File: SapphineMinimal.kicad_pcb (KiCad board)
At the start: 4 copper layers, 54.6 x 61 mm, 149 parts, among them IC301 DLHR-F50D-E1BD-C-NAV8, J201 JST, J401 503182-1852, J501 Conn_02x05_Odd_Even, J502 Conn_01x03_Male, J503 USB_B_Micro, J504 Conn_01x05_Male, J505 Conn_01x08_Female, J506 Conn_01x08_Female, J507 Conn_01x04_Male, J701 Conn_01x04_Male, J702 Conn_01x01_Male, J703 Conn_01x06_Male, Q201 BC857BS, Q202 IRLML6402TRPBF, SW501 EVQP7C01P, SW601 EVQP7C01P, U201 TPS62150, U202 INA219BIDR, U301 LIS331DLHTR, U401 TPS22860DBVR, U501 ATSAMD21E18A-AUT, U502 BMP388, U503 MB85RS1MT, U601 DS3231SN, U701 TPS22860DBVR

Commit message: 3d references'
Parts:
- SW501, SW601: value EVQP7C01P -> EVQP7C/L_PAN
- U301: value LIS331DLHTR -> LGA-16_3x3x1mm_STM
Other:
- net class Default removed
- net class Ground removed
- net class Power removed

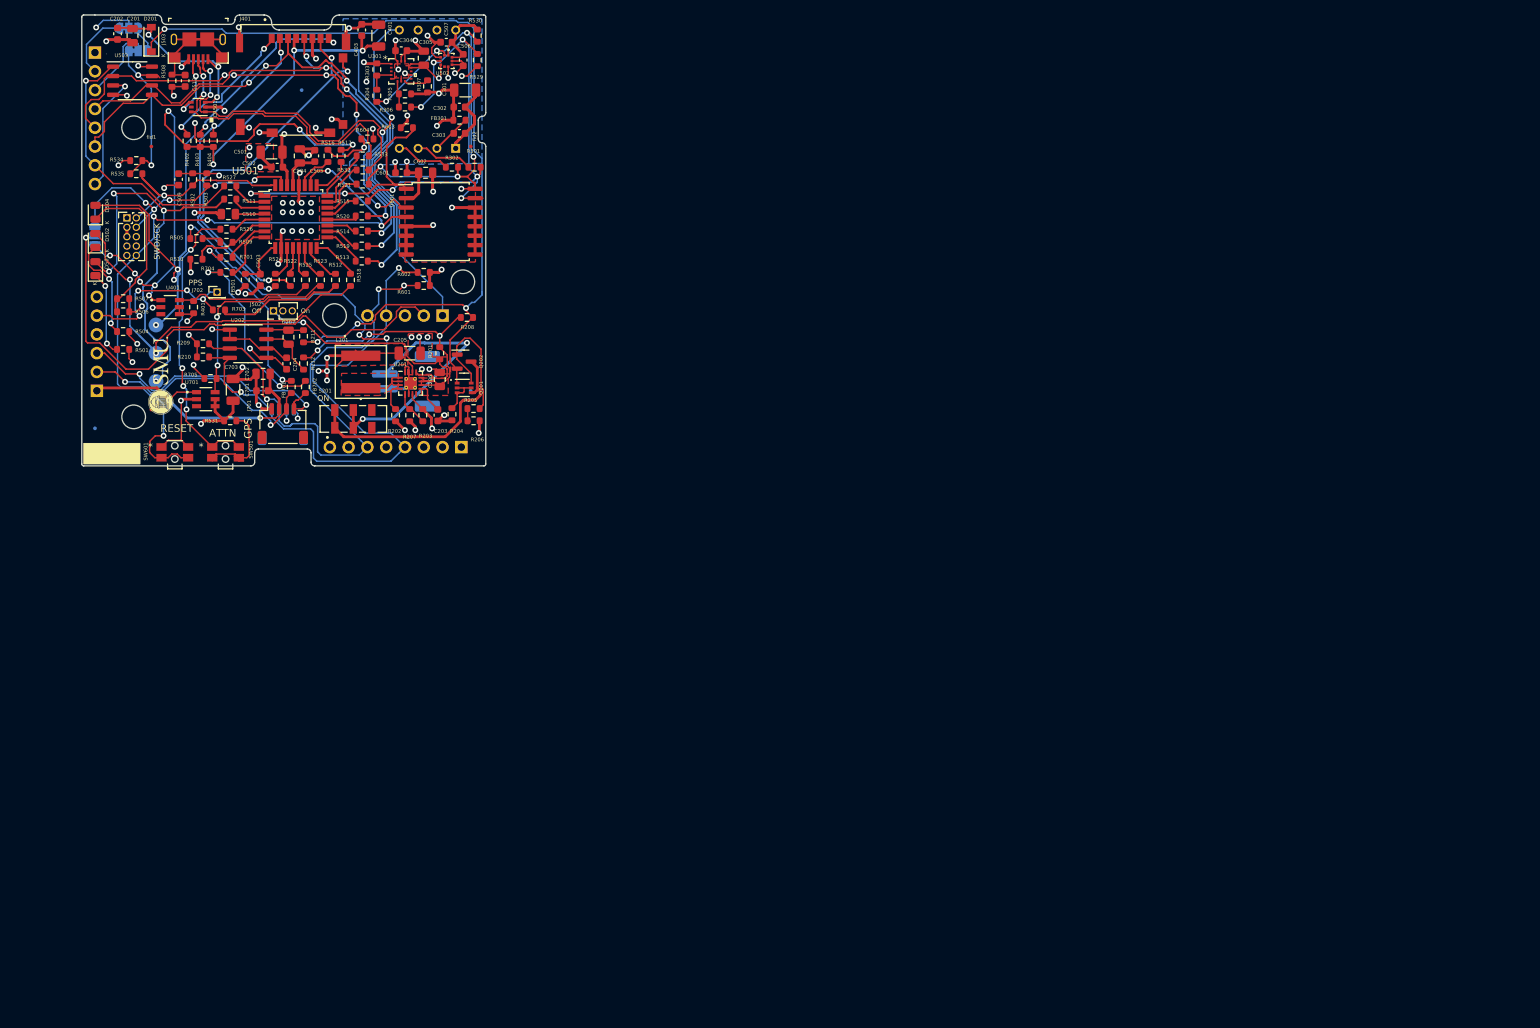
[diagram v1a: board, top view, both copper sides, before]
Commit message: Footprints complete. Starting layout
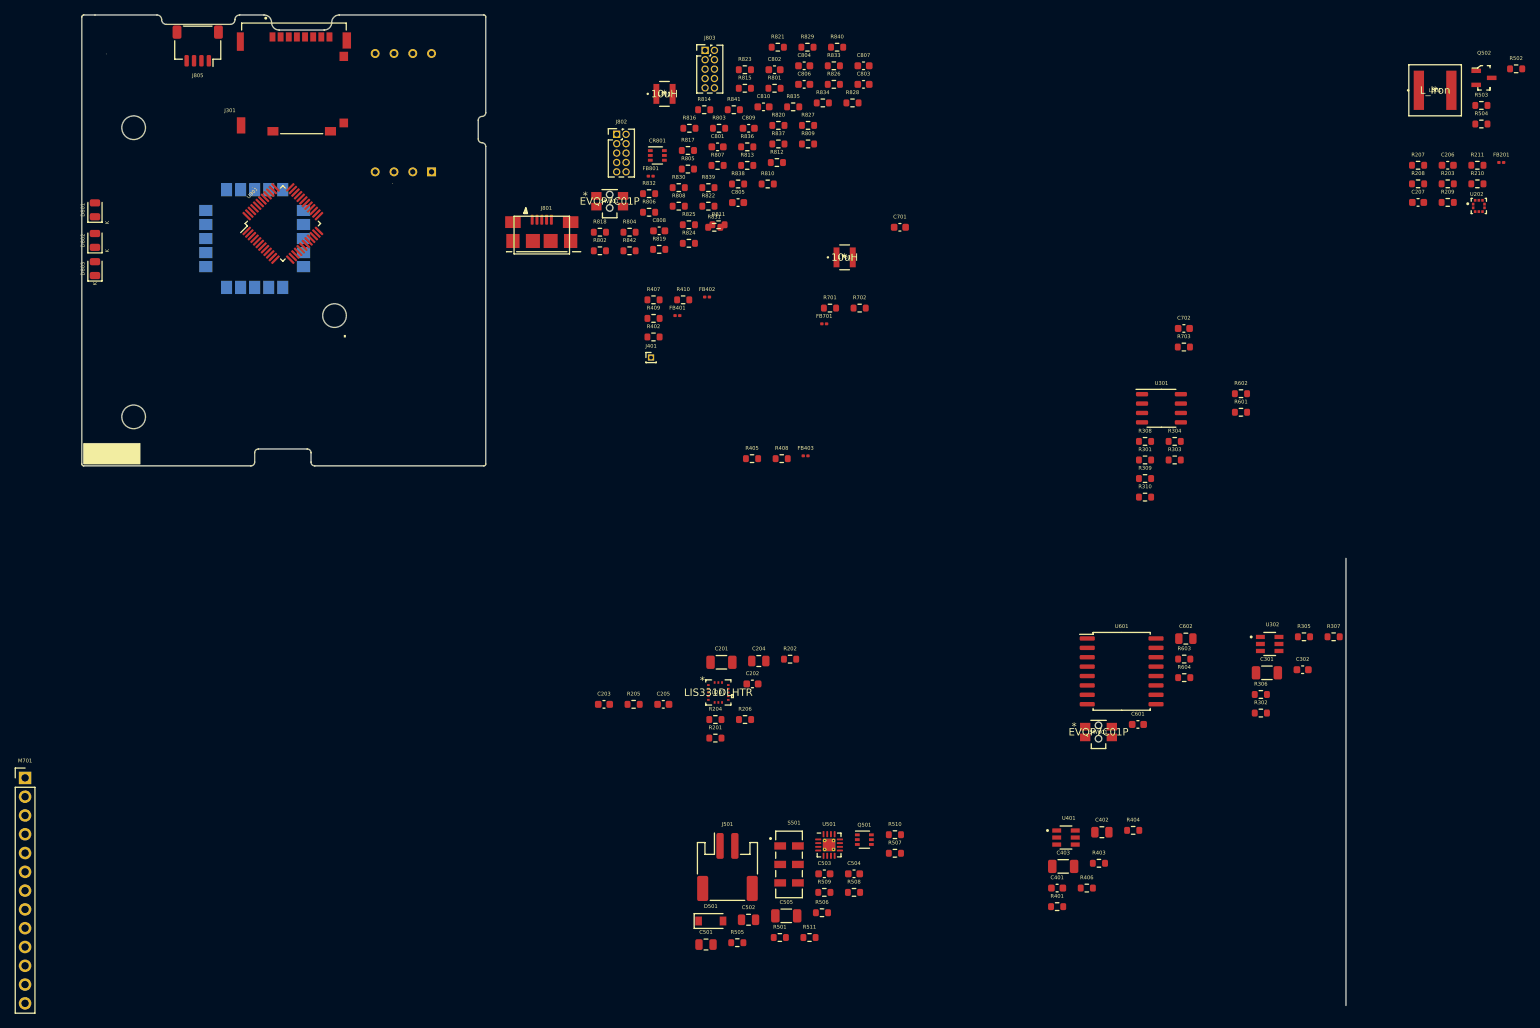
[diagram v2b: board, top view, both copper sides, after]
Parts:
- removed C303, C304, C506, C507, C509, C512: 100nF, Capacitor_SMD:C_0603_1608Metric
- removed C305: 10uF, Capacitor_SMD:C_0805_2012Metric
- removed C510: 1uF, Capacitor_SMD:C_0805_2012Metric
- removed C703: 22uF, Capacitor_SMD:C_1206_3216Metric
- removed CR501: TPD4E1U06DCKR, Package_TO_SOT_SMD:SOT-363_SC-70-6
- removed D201: MBR180, Diode_SMD:D_SOD-123
- removed D502: RED LED, LED_SMD:LED_0805_2012Metric
- removed D504: GREEN LED, LED_SMD:LED_0805_2012Metric
- removed FB301, FB501, FB702: 600, Resistor_SMD:R_0603_1608Metric
- removed G***: LOGO, LOGOS:SMU_Logo
- removed G***: LOGO, SapphineMinimal:SMU_Logo_Big2
- removed IC301: DLHR-F50D-E1BD-C-NAV8, SapphineMinimal:DLHRF50DE1BDCNAV8
- removed J201: JST, Connector_JST:JST_PH_S2B-PH-SM4-TB_1x02-1MP_P2.00mm_Horizontal
- removed J502: Conn_01x03_Male, Connector_PinHeader_1.27mm:PinHeader_1x03_P1.27mm_Vertical
- removed J503: USB_B_Micro, digikey-footprints:USB_Micro_B_Female_10118193-0001LF
- removed J504: Conn_01x05_Male, Connector_PinSocket_2.54mm:PinSocket_1x05_P2.54mm_Vertical
- removed J505, J506: Conn_01x08_Female, Connector_PinSocket_2.54mm:PinSocket_1x08_P2.54mm_Vertical
- removed J507, J701: Conn_01x04_Male, Connector_JST:JST_SH_SM04B-SRSS-TB_1x04-1MP_P1.00mm_Horizontal
- removed J702: Conn_01x01_Male, Connector_PinHeader_1.27mm:PinHeader_1x01_P1.27mm_Vertical
- removed J703: Conn_01x06_Male, Connector_PinHeader_2.54mm:PinHeader_1x06_P2.54mm_Horizontal
- removed JP501, JP502: Jumper_3_Bridged12, Jumper:SolderJumper-3_P1.3mm_Bridged12_RoundedPad1.0x1.5mm_NumberLabels
- removed JP503: SolderJumper_3_Open, Jumper:SolderJumper-3_P1.3mm_Open_RoundedPad1.0x1.5mm_NumberLabels
- removed L201: 2.2uH, SapphineMinimal:74439344022
- removed Q201: BC857BS, Package_TO_SOT_SMD:SOT-363_SC-70-6
- removed Q202: IRLML6402TRPBF, Package_TO_SOT_SMD:SOT-23
- removed R212: 10, Resistor_SMD:R_0603_1608Metric
- removed R512, R513, R515, R516, R517, R518, R519, R520, R521, R523, R524, R525, R526, R527, R532, R533, R535, R704: 47, Resistor_SMD:R_0603_1608Metric
- removed R514, R522, R531: 2K, Resistor_SMD:R_0603_1608Metric
- removed R529, R530: 4K75, Resistor_SMD:R_0603_1608Metric
- removed R534: 10K, Resistor_SMD:R_0603_1608Metric
- removed R705: 100K, Resistor_SMD:R_0603_1608Metric
- removed the REF** at (128.5, 102.1)
- removed S201: JS202011JCQN, SapphineMinimal:SW_JS202011JCQN
- removed SW501: EVQP7C/L_PAN, SapphineMinimal:EVQP7C01P
- removed TP501, TP502, TP503: TestPoint, TestPoint:TestPoint_Pad_D2.0mm
- removed U502: BMP388, SapphineMinimal:PQFN50P200X200X80-10N
- removed U503: MB85RS1MT, Package_SO:SOP-8_3.9x4.9mm_P1.27mm
- removed U701: TPS22860DBVR, SapphineMinimal:SOT95P280X145-6N
- removed fid1 (x2), fid2, fid4, fid5, fid6: Fiducial_0.5mm_Mask1mm, Fiducial:Fiducial_0.5mm_Mask1mm
- added C402: 10uF, Capacitor_SMD:C_0805_2012Metric, F.Cu at (214.9, 176.5)
- added C801: 100nF, Capacitor_SMD:C_0603_1608Metric, F.Cu at (162.9, 83.9)
- added C802: 1uf, Capacitor_SMD:C_0603_1608Metric, F.Cu at (170.6, 73.4)
- added C803: 100pF, Capacitor_SMD:C_0603_1608Metric, F.Cu at (182.6, 75.4)
- added C804: 1uf, Capacitor_SMD:C_0603_1608Metric, F.Cu at (174.6, 72.9)
- added C805: 22uF, Capacitor_SMD:C_0603_1608Metric, F.Cu at (165.7, 91.4)
- added C806: 100nF, Capacitor_SMD:C_0603_1608Metric, F.Cu at (174.6, 75.4)
- added C807: 100nF, Capacitor_SMD:C_0603_1608Metric, F.Cu at (182.6, 72.9)
- added C808: 22uF, Capacitor_SMD:C_0603_1608Metric, F.Cu at (155.0, 95.2)
- added C809: 100nF, Capacitor_SMD:C_0603_1608Metric, F.Cu at (167.1, 81.4)
- added C810: 100nF, Capacitor_SMD:C_0603_1608Metric, F.Cu at (169.1, 78.5)
- added CR801: TPD4E1U06DCKR, Package_TO_SOT_SMD:SOT-363_SC-70-6, F.Cu at (154.8, 85.0)
- added D801: RED LED, LED_SMD:LED_0805_2012Metric, F.Cu at (78.7, 92.4)
- added D802: RED LED, LED_SMD:LED_0805_2012Metric, F.Cu at (78.7, 96.5)
- added D803: GREEN LED, LED_SMD:LED_0805_2012Metric, F.Cu at (78.7, 100.3)
- added FB201: FerriteBead, Inductor_SMD:L_0201_0603Metric, F.Cu at (268.9, 86.0)
- added FB401: FerriteBead, Inductor_SMD:L_0201_0603Metric, F.Cu at (157.5, 106.7)
- added FB402: FerriteBead, Inductor_SMD:L_0201_0603Metric, F.Cu at (161.5, 104.2)
- added FB403: FerriteBead, Inductor_SMD:L_0201_0603Metric, F.Cu at (174.8, 125.6)
- added FB801: FerriteBead, Inductor_SMD:L_0201_0603Metric, F.Cu at (153.9, 87.8)
- added IC201: DLHR-F50D-E1BD-C-NAV8, SapphineMinimal:DLHRF50DE1BDCNAV8, B.Cu at (124.2, 87.2)
- added J301: 503182-1852, SapphineMinimal:MOLEX_503182-1852, F.Cu at (105.6, 75.4)
- added J801: USB_B_Micro, SapphineMinimal:uUSB_B, F.Cu at (139.1, 96.6)
- added J802: Conn_02x05_Odd_Even, Connector_PinHeader_1.27mm:PinHeader_2x05_P1.27mm_Vertical, F.Cu at (149.3, 82.2)
- added J803: Conn_02x05_Odd_Even, Connector_PinHeader_1.27mm:PinHeader_2x05_P1.27mm_Vertical, F.Cu at (161.2, 70.8)
- added J805: Conn_01x04_Male, Connector_JST:JST_SH_SM04B-SRSS-TB_1x04-1MP_P1.00mm_Horizontal, F.Cu at (92.6, 70.2)
- added L501: L_Iron, SapphineMinimal:74439344022, F.Cu at (259.9, 76.2)
- added L701: 10uH, SapphineMinimal:NR3012T100M, F.Cu at (180.1, 98.8)
- added L801: 10uH, SapphineMinimal:NR3012T100M, F.Cu at (155.7, 76.7)
- added M701: AdafruitWINC1500, Connector_PinHeader_2.54mm:PinHeader_1x13_P2.54mm_Vertical, F.Cu at (69.3, 169.2)
- added Q501: BC857BS, Package_TO_SOT_SMD:SOT-363_SC-70-6, F.Cu at (182.8, 177.5)
- added Q502: IRLML6402TRPBF, digikey-footprints:SOT-23-3, F.Cu at (266.5, 74.5)
- added R308: 47, Resistor_SMD:R_0603_1608Metric, F.Cu at (220.7, 123.7)
- added R309: 47, Resistor_SMD:R_0603_1608Metric, F.Cu at (220.7, 128.7)
- added R310: 0, Resistor_SMD:R_0603_1608Metric, F.Cu at (220.7, 131.2)
- added R405: 47, Resistor_SMD:R_0603_1608Metric, F.Cu at (167.6, 126.0)
- added R406: 100K, Resistor_SMD:R_0603_1608Metric, F.Cu at (212.8, 184.1)
- added R407: 47, Resistor_SMD:R_0603_1608Metric, F.Cu at (154.2, 104.5)
- added R408: 47, Resistor_SMD:R_0603_1608Metric, F.Cu at (171.6, 126.0)
- added R409: open, Resistor_SMD:R_0603_1608Metric, F.Cu at (154.2, 107.1)
- added R410: open, Resistor_SMD:R_0603_1608Metric, F.Cu at (158.3, 104.5)
- added R702: 47, Resistor_SMD:R_0603_1608Metric, F.Cu at (182.1, 105.7)
- added R801: 4K75, Resistor_SMD:R_0603_1608Metric, F.Cu at (170.6, 76.0)
- added R802: 2K, Resistor_SMD:R_0603_1608Metric, F.Cu at (147.0, 97.9)
- added R803: 2K, Resistor_SMD:R_0603_1608Metric, F.Cu at (163.1, 81.4)
- added R804: 2K, Resistor_SMD:R_0603_1608Metric, F.Cu at (151.0, 95.4)
- added R805: 2K, Resistor_SMD:R_0603_1608Metric, F.Cu at (158.9, 86.9)
- added R806: 2K, Resistor_SMD:R_0603_1608Metric, F.Cu at (153.7, 92.7)
- added R807: 4K75, Resistor_SMD:R_0603_1608Metric, F.Cu at (162.9, 86.4)
- added R808: 4K75, Resistor_SMD:R_0603_1608Metric, F.Cu at (157.7, 91.9)
- added R809: 47, Resistor_SMD:R_0603_1608Metric, F.Cu at (175.1, 83.5)
- added R810: 330, Resistor_SMD:R_0603_1608Metric, F.Cu at (169.7, 88.9)
- added R811: 2k2, Resistor_SMD:R_0603_1608Metric, F.Cu at (163.0, 94.4)
- added R812: 47, Resistor_SMD:R_0603_1608Metric, F.Cu at (170.9, 86.0)
- added R813: 47, Resistor_SMD:R_0603_1608Metric, F.Cu at (166.9, 86.4)
- added R814: 47, Resistor_SMD:R_0603_1608Metric, F.Cu at (161.1, 78.8)
- added R815: 47, Resistor_SMD:R_0603_1608Metric, F.Cu at (166.6, 76.0)
- added R816: 47, Resistor_SMD:R_0603_1608Metric, F.Cu at (159.1, 81.4)
- added R817: 47, Resistor_SMD:R_0603_1608Metric, F.Cu at (158.9, 84.4)
- added R818: 47, Resistor_SMD:R_0603_1608Metric, F.Cu at (147.0, 95.4)
- added R819: 47, Resistor_SMD:R_0603_1608Metric, F.Cu at (155.0, 97.7)
- added R820: 47, Resistor_SMD:R_0603_1608Metric, F.Cu at (171.1, 81.0)
- added R821: 47, Resistor_SMD:R_0603_1608Metric, F.Cu at (171.1, 70.4)
- added R822: 47, Resistor_SMD:R_0603_1608Metric, F.Cu at (161.7, 91.9)
- added R823: 47, Resistor_SMD:R_0603_1608Metric, F.Cu at (166.6, 73.4)
- added R824: 47, Resistor_SMD:R_0603_1608Metric, F.Cu at (159.0, 96.9)
- added R825: 47, Resistor_SMD:R_0603_1608Metric, F.Cu at (159.0, 94.4)
- added R826: 47, Resistor_SMD:R_0603_1608Metric, F.Cu at (178.6, 75.4)
- added R827: 47, Resistor_SMD:R_0603_1608Metric, F.Cu at (175.1, 81.0)
- added R828: 47, Resistor_SMD:R_0603_1608Metric, F.Cu at (181.2, 77.9)
- added R829: 47, Resistor_SMD:R_0603_1608Metric, F.Cu at (175.1, 70.4)
- added R830: 47, Resistor_SMD:R_0603_1608Metric, F.Cu at (157.7, 89.4)
- added R831: 47, Resistor_SMD:R_0603_1608Metric, F.Cu at (162.5, 94.7)
- added R832: 47, Resistor_SMD:R_0603_1608Metric, F.Cu at (153.7, 90.2)
- added R833: 47, Resistor_SMD:R_0603_1608Metric, F.Cu at (178.6, 72.9)
- added R834: 47, Resistor_SMD:R_0603_1608Metric, F.Cu at (177.1, 77.9)
- added R835: 47, Resistor_SMD:R_0603_1608Metric, F.Cu at (173.1, 78.5)
- added R836: 47, Resistor_SMD:R_0603_1608Metric, F.Cu at (166.9, 83.9)
- added R837: 47, Resistor_SMD:R_0603_1608Metric, F.Cu at (171.1, 83.5)
- added R838: 47, Resistor_SMD:R_0603_1608Metric, F.Cu at (165.7, 88.9)
- added R839: 47, Resistor_SMD:R_0603_1608Metric, F.Cu at (161.7, 89.4)
- added R840: 47, Resistor_SMD:R_0603_1608Metric, F.Cu at (179.1, 70.4)
- added R841: 1k0, Resistor_SMD:R_0603_1608Metric, F.Cu at (165.1, 78.8)
- added R842: 47K5, Resistor_SMD:R_0603_1608Metric, F.Cu at (151.0, 97.9)
- added S501: JS202011JCQN, SapphineMinimal:SW_JS202011JCQN, F.Cu at (172.6, 180.9)
- added SW801: EVQP7C01P, SapphineMinimal:EVQP7C01P, F.Cu at (148.3, 91.2)
- added U302: TPS22860DBVR, SapphineMinimal:SOT95P280X145-6N, F.Cu at (237.6, 151.1)
- added U402: SAM-M8Q-0-10, SapphineMinimal:MODULE_SAM-M8Q-0-10, B.Cu at (100.3, 96.3)
- added U801: ATSAMD21G18A-A, Package_QFP:TQFP-48_7x7mm_P0.5mm, F.Cu at (104.1, 94.2)
- C201: value 10uF -> 22uF; footprint Capacitor_SMD:C_0805_2012Metric -> Capacitor_SMD:C_1206_3216Metric
- C203: value 390pF -> 100nF
- C204, C502: value 100nF -> 10uF; footprint Capacitor_SMD:C_0603_1608Metric -> Capacitor_SMD:C_0805_2012Metric
- C205, C401: value 22uF -> 100nF; footprint Capacitor_SMD:C_1206_3216Metric -> Capacitor_SMD:C_0603_1608Metric
- C206: value 10uF -> 100nF; footprint Capacitor_SMD:C_0805_2012Metric -> Capacitor_SMD:C_0603_1608Metric
- C207, C702: value 1uF -> 100nF; footprint Capacitor_SMD:C_0805_2012Metric -> Capacitor_SMD:C_0603_1608Metric
- C403, C505: value 100nF -> 22uF; footprint Capacitor_SMD:C_0603_1608Metric -> Capacitor_SMD:C_1206_3216Metric
- C501: value 22uF -> 10uF; footprint Capacitor_SMD:C_1206_3216Metric -> Capacitor_SMD:C_0805_2012Metric
- C504: value 1uF -> 390pF; footprint Capacitor_SMD:C_0805_2012Metric -> Capacitor_SMD:C_0603_1608Metric
- C701: value 100nF -> 22uF
- D501: value RED LED -> MBR180; footprint LED_SMD:LED_0805_2012Metric -> Diode_SMD:D_SOD-123
- FB701: value 600 -> FerriteBead; footprint Resistor_SMD:R_0603_1608Metric -> Inductor_SMD:L_0201_0603Metric
- J401: value 503182-1852 -> Conn_01x01_Male; footprint Custom_footprints:MOLEX_503182-1852 -> Connector_PinHeader_1.00mm:PinHeader_1x01_P1.00mm_Vertical
- J501: value Conn_02x05_Odd_Even -> JST; footprint Connector_PinHeader_1.27mm:PinHeader_2x05_P1.27mm_Vertical -> Connector_JST:JST_PH_S2B-PH-SM4-TB_1x02-1MP_P2.00mm_Horizontal
- R201, R202, R204, R205, R401, R403: value 100K -> 47
- R203: value 562K -> 47
- R206: value 47K5 -> 10K
- R207: value 180K -> 47
- R208: value 0.1 -> 47
- R209, R210, R303: value 10K -> 47
- R211: value 10 -> 0
- R301: value 47 -> 10K
- R302, R306: value 47 -> 100K
- R305: value 10K -> 100K
- R307: value 10K -> 47K5
- R402: value 100K -> 0R25
- R404: value 47K5 -> 47
- R501: value 2K -> 100K
- R502, R503: value 47K5 -> 100K
- R504, R506: value 2K -> 47K5
- R507: value 2K -> 0
- R508: value 4K75 -> 100K
- R510: value 47K5 -> 562K
- R511: value 47 -> 180K
- R601, R602: value 4K75 -> 47
- R701: value 47 -> 0R25
- SW601: value EVQP7C/L_PAN -> EVQP7C01P
- U201: value TPS62150 -> LIS331DLHTR; footprint Package_DFN_QFN:VQFN-16-1EP_3x3mm_P0.5mm_EP1.68x1.68mm_ThermalVias -> SapphineMinimal:LIS331DLHTR
- U202: value INA219BIDR -> BMP388; footprint Package_SO:SOIC-8_3.9x4.9mm_P1.27mm -> SapphineMinimal:PQFN50P200X200X80-10N
- U301: value LGA-16_3x3x1mm_STM -> MB85RS1MT; footprint SapphineMinimal:LIS331DLHTR -> Package_SO:SOP-8_3.9x4.9mm_P1.27mm
- U501: value ATSAMD21E18A-AUT -> TPS62150; footprint Package_QFP:TQFP-32_7x7mm_P0.8mm -> Package_DFN_QFN:VQFN-16-1EP_3x3mm_P0.5mm_EP1.68x1.68mm_ThermalVias
- moved R504 185.8 mm to (266.2, 80.8)
- moved R502 179.5 mm to (270.9, 73.3), turned to 0 degrees
- moved R210 173.9 mm to (265.6, 88.9)
- moved R503 172.6 mm to (266.2, 78.3), turned to 0 degrees
- moved R209 169.4 mm to (261.6, 91.4)
- moved U202 167.4 mm to (265.8, 91.9)
- moved R211 160.4 mm to (265.6, 86.4), turned to 0 degrees
- moved R403 155.9 mm to (214.5, 180.7), turned to 0 degrees
- moved R404 155.4 mm to (219.1, 176.3), turned to 0 degrees
- moved C207 153.8 mm to (257.6, 91.4), turned to 0 degrees
- moved C403 147.6 mm to (209.6, 181.1), turned to 0 degrees
- moved C401 147.3 mm to (208.8, 184.1), turned to 0 degrees
- moved R307 143.3 mm to (246.2, 150.1), turned to 0 degrees
- moved R508 143.3 mm to (181.4, 184.7), turned to 0 degrees
- moved R401 142.1 mm to (208.8, 186.6), turned to 0 degrees
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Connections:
- net /SapphireMini_Proc/LOCAL_PPS renamed /Sapphire_Proc/LOCAL_PPS
- C201 pad 1: /SapphireMini_Proc/VBUS -> /P3V3
- C202 pad 1: /SapphireMini_Proc/VBUS -> /P3V3
- C206 pad 1: /SapphireMini_Power/PWR_IN -> /P3V3
- C207 pad 1: Net-(C207-Pad1) -> /P3V3
- C207 pad 2: Net-(C207-Pad2) -> GND
- C301 pad 1: /P3V3 -> Net-(C301-Pad1)
- C302 pad 1: /P3V3 -> Net-(C301-Pad1)
- C401 pad 1: /SapphireMini_Proc/SD_SWITCHED_PWR -> /SapphireMini_GNSS/GNSS_POWER_OUT
- C403 pad 1: /SapphireMini_Proc/SD_SWITCHED_PWR -> /P3V3
- C501 pad 1: /P3V3 -> /SapphireMini_Power/VBUS
- C502 pad 1: /P3V3 -> /SapphireMini_Power/PWR_IN
- C503 pad 1: Net-(C503-Pad1) -> /SapphireMini_Power/VBUS
- C505 pad 1: Net-(C504-Pad1) -> /P3V3
- C702 pad 1: Net-(C701-Pad1) -> Net-(C702-Pad1)
- D501 pad 2: /SapphireMini_Proc/RED_LED -> /SapphireMini_Power/VBUS
- FB701 pad 1: Net-(FB701-Pad1) -> Net-(C701-Pad1)
- J501 pad 1: /P3V3 -> Net-(J501-Pad1)
- J501 pad 2: /SapphireMini_Proc/SWDIO -> GND
- R201 pad 1: /SapphireMini_Power/PWR_IN -> Net-(R201-Pad1)
- R201 pad 2: /SapphireMini_Power/VBAT_EN -> /SapphireMini_DLHR/I2C_SCL
- R202 pad 1: /P3V3 -> Net-(R202-Pad1)
- R202 pad 2: Net-(R202-Pad2) -> /SapphireMini_DLHR/I2C_SDA
- R203 pad 1: /P3V3 -> Net-(R203-Pad1)
- R203 pad 2: Net-(R203-Pad2) -> GND
- R204 pad 2: GND -> /SapphireMini_DLHR/I2C_SDA
- R205 pad 2: Net-(R205-Pad2) -> /SapphireMini_DLHR/I2C_SCL
- R206 pad 1: Net-(R205-Pad2) -> Net-(R206-Pad1)
- R206 pad 2: GND -> /P3V3
- R207 pad 1: Net-(R203-Pad2) -> /Sapphire_Proc/ACC_INT1
- R207 pad 2: GND -> Net-(R207-Pad2)
- R208 pad 1: Net-(D201-Pad1) -> /Sapphire_Proc/ACC_INT2
- R208 pad 2: /SapphireMini_Power/PWR_IN -> Net-(R208-Pad2)
- R209 pad 1: /P3V3 -> Net-(R209-Pad1)
- R209 pad 2: /SapphireMini_DLHR/I2C_SDA -> /SapphireMini_DLHR/I2C_SCL
- R210 pad 1: /P3V3 -> Net-(R210-Pad1)
- R210 pad 2: /SapphireMini_DLHR/I2C_SCL -> /SapphireMini_DLHR/I2C_SDA
- R211 pad 1: Net-(C207-Pad1) -> Net-(R211-Pad1)
- R211 pad 2: Net-(D201-Pad1) -> GND
- R301 pad 1: Net-(IC301-Pad3) -> /SapphireMini_SD/FRAM_HOLD
- R301 pad 2: /SapphireMini_DLHR/I2C_SDA -> /P3V3
- R302 pad 1: Net-(IC301-Pad4) -> /Sapphire_Proc/SD_PWR
- R302 pad 2: /SapphireMini_DLHR/I2C_SCL -> /P3V3
- R303 pad 1: Net-(R303-Pad1) -> /SapphireMini_SD/SPI_SCK
- R303 pad 2: /P3V3 -> Net-(R303-Pad2)
- R304 pad 1: Net-(R303-Pad1) -> /SapphireMini_SD/SPI_MOSI
- R304 pad 2: /SapphireMini_DLHR/I2C_SCL -> Net-(R304-Pad2)
- R305 pad 1: Net-(R305-Pad1) -> Net-(J301-Pad1)
- R305 pad 2: /P3V3 -> Net-(C301-Pad1)
- R306 pad 1: Net-(R305-Pad1) -> Net-(C301-Pad1)
- R306 pad 2: /SapphireMini_DLHR/I2C_SDA -> Net-(J301-Pad8)
- R307 pad 1: Net-(R307-Pad1) -> Net-(C301-Pad1)
- R307 pad 2: /P3V3 -> /Sapphire_Proc/SD_CS
- R401 pad 1: /SapphireMini_Proc/SD_PWR -> /Sapphire_Proc/TIMEMARK
- R401 pad 2: /P3V3 -> Net-(R401-Pad2)
- R402 pad 1: Net-(J401-Pad1) -> /SapphireMini_GNSS/GNSS_POWER_OUT
- R402 pad 2: /SapphireMini_Proc/SD_SWITCHED_PWR -> Net-(FB401-Pad1)
- R403 pad 1: /SapphireMini_Proc/SD_SWITCHED_PWR -> /Sapphire_Proc/RS232_TXD5
- R403 pad 2: Net-(J401-Pad8) -> Net-(FB403-Pad1)
- R404 pad 1: /SapphireMini_Proc/SD_SWITCHED_PWR -> Net-(FB402-Pad1)
- R404 pad 2: /SapphireMini_Proc/SD_CS -> /Sapphire_Proc/RS232_RXD5
- R501 pad 1: Net-(D501-Pad1) -> Net-(Q501-Pad2)
- R502 pad 1: /SapphireMini_Proc/SWDIO -> /SapphireMini_Power/VBAT
- R502 pad 2: /P3V3 -> Net-(R502-Pad2)
- R503 pad 1: /SapphireMini_Proc/SWCLK -> Net-(R502-Pad2)
- R503 pad 2: /P3V3 -> /SapphireMini_Power/VBAT_MON
- R504 pad 1: Net-(D502-Pad1) -> /SapphireMini_Power/VBAT_MON
- R505 pad 1: /SapphireMini_Power/VBAT -> Net-(Q501-Pad6)
- R506 pad 1: Net-(D504-Pad1) -> Net-(R505-Pad2)
- R507 pad 1: Net-(D504-Pad1) -> Net-(D501-Pad1)
- R507 pad 2: GND -> /SapphireMini_Power/PWR_IN
- R508 pad 1: GND -> /SapphireMini_Power/PWR_IN
- R508 pad 2: Net-(C512-Pad1) -> /SapphireMini_Power/VBAT_EN
- R509 pad 1: Net-(R505-Pad2) -> /P3V3
- R509 pad 2: /SapphireMini_Proc/VBAT_MON -> Net-(R509-Pad2)
- R510 pad 1: /SapphireMini_Proc/VBAT_MON -> /P3V3
- R510 pad 2: GND -> Net-(R510-Pad2)
- R511 pad 1: Net-(R511-Pad1) -> Net-(R510-Pad2)
- R511 pad 2: /SapphireMini_Proc/RED_LED -> GND
- R601 pad 1: /P3V3 -> Net-(R601-Pad1)
- R601 pad 2: /SapphireMini_DLHR/I2C_SDA -> /SapphireMini_DLHR/I2C_SCL
- R602 pad 1: /P3V3 -> Net-(R602-Pad1)
- R602 pad 2: /SapphireMini_DLHR/I2C_SCL -> /SapphireMini_DLHR/I2C_SDA
- R603 pad 2: /SapphireMini_DS3231/32KHz -> /Sapphire_Proc/32KHz
- R701 pad 2: /SapphireMini_GNSS/RS232_RXD -> Net-(C702-Pad1)
- R703 pad 1: /SapphireMini_GNSS/TIMEMARK -> Net-(M701-Pad5)
- R703 pad 2: Net-(J702-Pad1) -> /SapphireMini_SD/SPI_MOSI
- SW601 pad 2: /SapphireMini_DS3231/RESET -> /Sapphire_Proc/RESET
- SW601 pad 3: /SapphireMini_DS3231/RESET -> /Sapphire_Proc/RESET
- U201 pad 1: Net-(L201-Pad1) -> /P3V3
- U201 pad 10: /SapphireMini_Power/PWR_IN -> GND
- U201 pad 11: /SapphireMini_Power/PWR_IN -> Net-(R207-Pad2)
- U201 pad 12: /SapphireMini_Power/PWR_IN -> GND
- U201 pad 13: /SapphireMini_Power/VBAT_EN -> GND
- U201 pad 15: GND -> /P3V3
- U201 pad 2: Net-(L201-Pad1) -> unconnected-(U201-Pad2)
- U201 pad 3: Net-(L201-Pad1) -> unconnected-(U201-Pad3)
- U201 pad 4: Net-(R202-Pad2) -> Net-(R201-Pad1)
- U201 pad 5: Net-(R203-Pad2) -> GND
- U201 pad 6: GND -> Net-(R202-Pad1)
- U201 pad 7: /P3V3 -> Net-(R203-Pad1)
- U201 pad 8: Net-(U201-Pad8) -> Net-(R206-Pad1)
- U201 pad 9: Net-(C203-Pad1) -> Net-(R208-Pad2)
- U202 pad 1: GND -> /P3V3
- U202 pad 2: GND -> Net-(R209-Pad1)
- U202 pad 3: /SapphireMini_DLHR/I2C_SDA -> GND
- U202 pad 4: /SapphireMini_DLHR/I2C_SCL -> Net-(R210-Pad1)
- U202 pad 5: /P3V3 -> Net-(R211-Pad1)
- U202 pad 6: GND -> unconnected-(U202-Pad6)
- U202 pad 7: Net-(C207-Pad2) -> /SapphireMini_DLHR/BMP_INT
- U202 pad 8: Net-(C207-Pad1) -> GND
- U301 pad 1: /P3V3 -> /SapphireMini_SD/FRAM_CS
- U301 pad 2: Net-(U301-Pad2) -> /SapphireMini_SD/SPI_MISO
- U301 pad 3: Net-(U301-Pad3) -> /SapphireMini_SD/FRAM_WP
- U301 pad 4: Net-(R303-Pad1) -> GND
- U301 pad 5: GND -> Net-(R304-Pad2)
- U301 pad 6: Net-(R305-Pad1) -> Net-(R303-Pad2)
- U301 pad 7: GND -> /SapphireMini_SD/FRAM_HOLD
- U301 pad 8: Net-(R307-Pad1) -> /P3V3
- U401 pad 1: /SapphireMini_Proc/SD_SWITCHED_PWR -> Net-(C402-Pad1)
- U401 pad 6: /SapphireMini_Proc/SD_PWR -> /Sapphire_Proc/GNSS_PWR
- U501 pad 1: /SapphireMini_DS3231/32KHz -> Net-(L501-Pad1)
- U501 pad 10: GND -> /SapphireMini_Power/PWR_IN
- U501 pad 11: Net-(R524-Pad1) -> /SapphireMini_Power/PWR_IN
- U501 pad 12: Net-(R522-Pad1) -> /SapphireMini_Power/PWR_IN
- U501 pad 13: Net-(R525-Pad1) -> /SapphireMini_Power/VBAT_EN
- U501 pad 14: Net-(R523-Pad1) -> /P3V3
- U501 pad 15: Net-(R512-Pad1) -> GND
- U501 pad 16: Net-(R518-Pad1) -> GND
- U501 pad 17: Net-(R513-Pad1) -> GND
- U501 pad 2: Net-(R527-Pad1) -> Net-(L501-Pad1)
- U501 pad 3: Net-(R511-Pad1) -> Net-(L501-Pad1)
- U501 pad 4: /SapphireMini_Proc/AREF -> Net-(R509-Pad2)
- U501 pad 5: Net-(R526-Pad1) -> Net-(R510-Pad2)
- U501 pad 6: /SapphireMini_Proc/VBAT_MON -> GND
- U501 pad 7: /SapphireMini_GNSS/RS232_RXD -> /P3V3
- U501 pad 8: /SapphireMini_Proc/RS232_RXD5 -> unconnected-(U501-Pad8)
- U501 pad 9: Net-(C503-Pad1) -> Net-(C504-Pad1)
- U601 pad 1: /SapphireMini_DS3231/32KHz -> /Sapphire_Proc/32KHz
- U601 pad 15: /SapphireMini_DLHR/I2C_SDA -> Net-(R602-Pad1)
- U601 pad 16: /SapphireMini_DLHR/I2C_SCL -> Net-(R601-Pad1)
- U601 pad 4: /SapphireMini_DS3231/RESET -> /Sapphire_Proc/RESET
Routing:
- net GND: track 194.7 -> 0.00 mm, vias 64 -> 0
- net /SapphireMini_DLHR/I2C_SCL: track 158.0 -> 0.00 mm, vias 9 -> 0
- net /SapphireMini_DLHR/I2C_SDA: track 147.9 -> 0.00 mm, vias 9 -> 0
- net /SapphireMini_Proc/SD_SWITCHED_PWR: track 129.6 -> 0.00 mm, vias 9 -> 0
- net /P3V3: track 129.2 -> 0.00 mm, vias 25 -> 0
- net Net-(D201-Pad1): track 122.9 -> 0.00 mm, vias 4 -> 0
- net /SapphireMini_DS3231/RESET: track 95.5 -> 0.00 mm, vias 5 -> 0
- net /SapphireMini_Proc/SPI_MOSI: track 81.1 -> 0.00 mm, vias 4 -> 0
- net /SapphireMini_Power/VBAT: track 78.0 -> 0.00 mm, vias 5 -> 0
- net /SapphireMini_Proc/GREEN_LED: track 77.6 -> 0.00 mm, vias 6 -> 0
- net /SapphireMini_Proc/BMP_INT: track 75.3 -> 0.00 mm, vias 1 -> 0
- net /SapphireMini_Proc/SPI_SCK: track 74.8 -> 0.00 mm, vias 4 -> 0
- net /SapphireMini_Proc/SPI_MISO: track 72.3 -> 0.00 mm, vias 6 -> 0
- net Net-(J504-Pad2): track 70.6 -> 0.00 mm, vias 1 -> 0
- net /SapphireMini_Proc/RED_LED: track 57.4 -> 0.00 mm, vias 4 -> 0
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- removed copper zone on F.Cu, net /P3V3
- removed copper zone on In2.Cu, net /P3V3
- removed copper zone on F.Cu, net /SapphireMini_Power/PWR_IN
- removed copper zone on B.Cu, net GND
- removed copper zone on F.Cu, net GND
- removed copper zone on In1.Cu, net GND
- removed copper zone on F.Cu, net Net-(L201-Pad1)
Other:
- board size 54.6 x 61 mm -> 170.9 x 133.9 mm
- board text removed: "+PWR"
- board text removed: "ATTN"
- board text removed: "Adafruit FRAM"
- board text removed: "BMP388"
- board text removed: "CS"
- board text removed: "GND"
- board text removed: "GNSS_PPS"
- board text removed: "GPS"
- board text removed: "HOLD"
- board text removed: "I2C STEMMA"
- board text removed: "I2C_SCL"
- board text removed: "I2C_SDA"
- board text removed: "LIS3DH"
- board text removed: "MISO"
- board text removed: "MOSI"
- board text removed: "NC"
- board text removed: "ON"
- board text removed: "Off"
- board text removed: "On"
- board text removed: "P3V3"
- board text removed: "PPS"
- board text removed: "RESET"
- board text removed: "RXD"
- board text removed: "SCK"
- board text removed: "SCL"
- board text removed: "SDA"
- board text removed: "SWD/SCK"
- board text removed: "Sapphire Mini Rev A July 18 2021"
- board text removed: "TXD"
- board text removed: "VBAT_EN"
- board text removed: "WP"
- board text removed: "hayward@smu.edu"

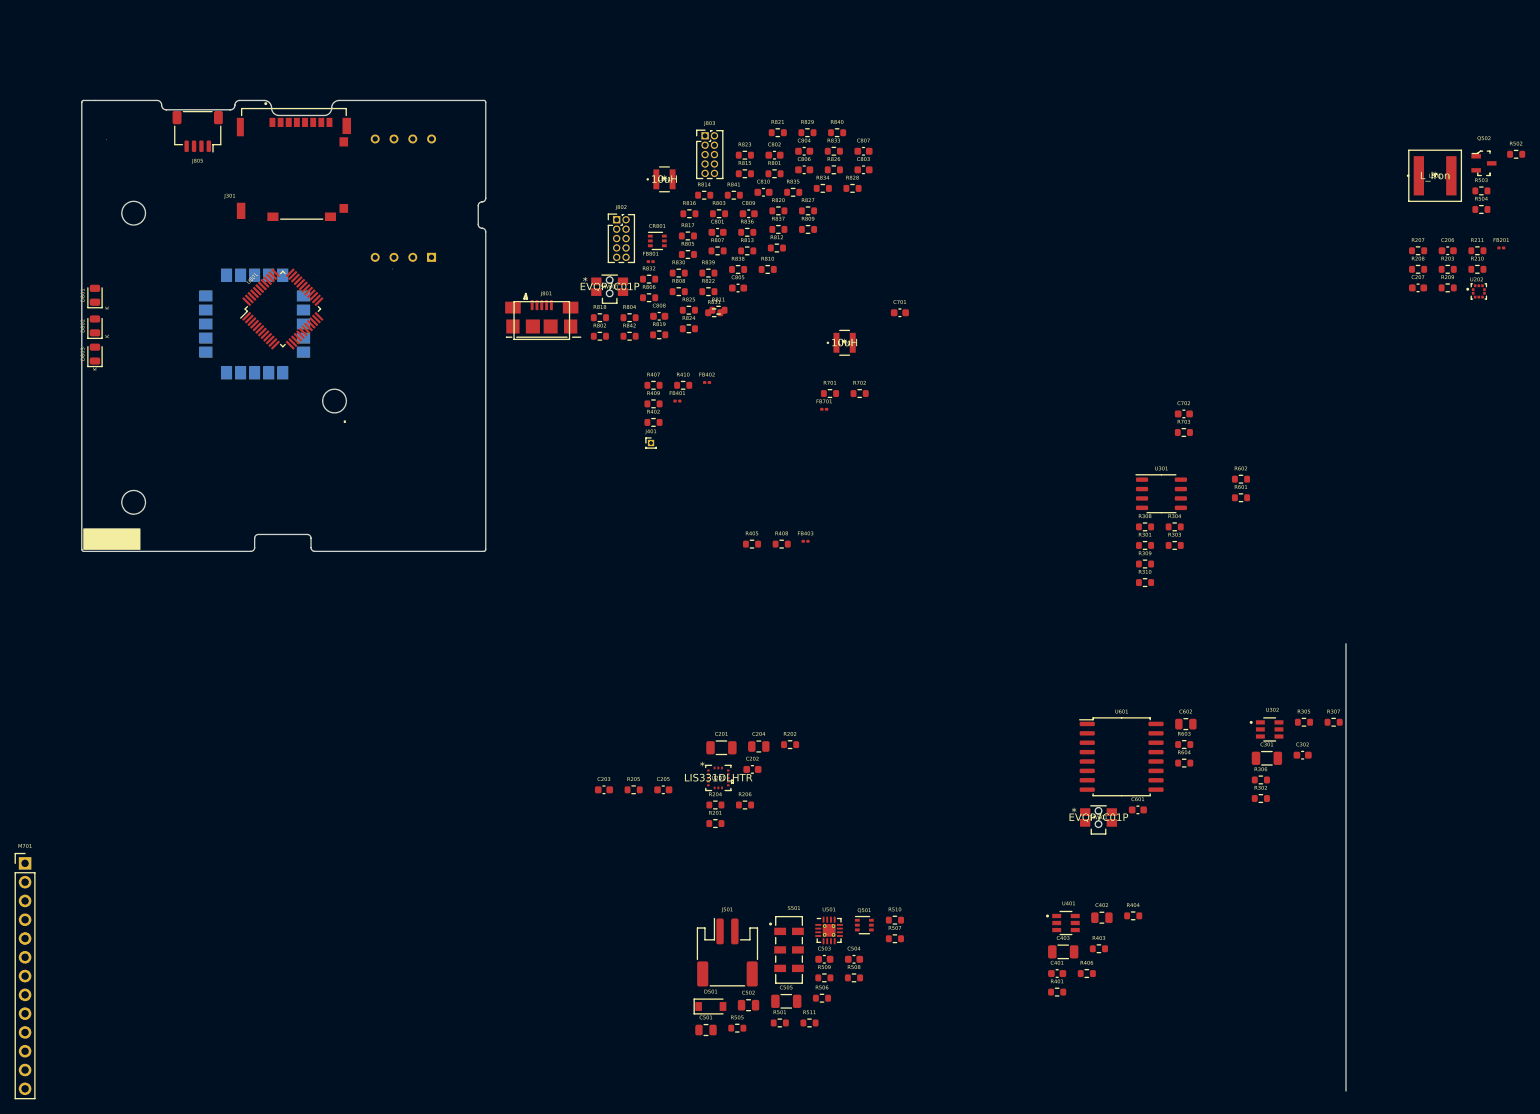
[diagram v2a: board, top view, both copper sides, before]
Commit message: replacing w/ resistor array
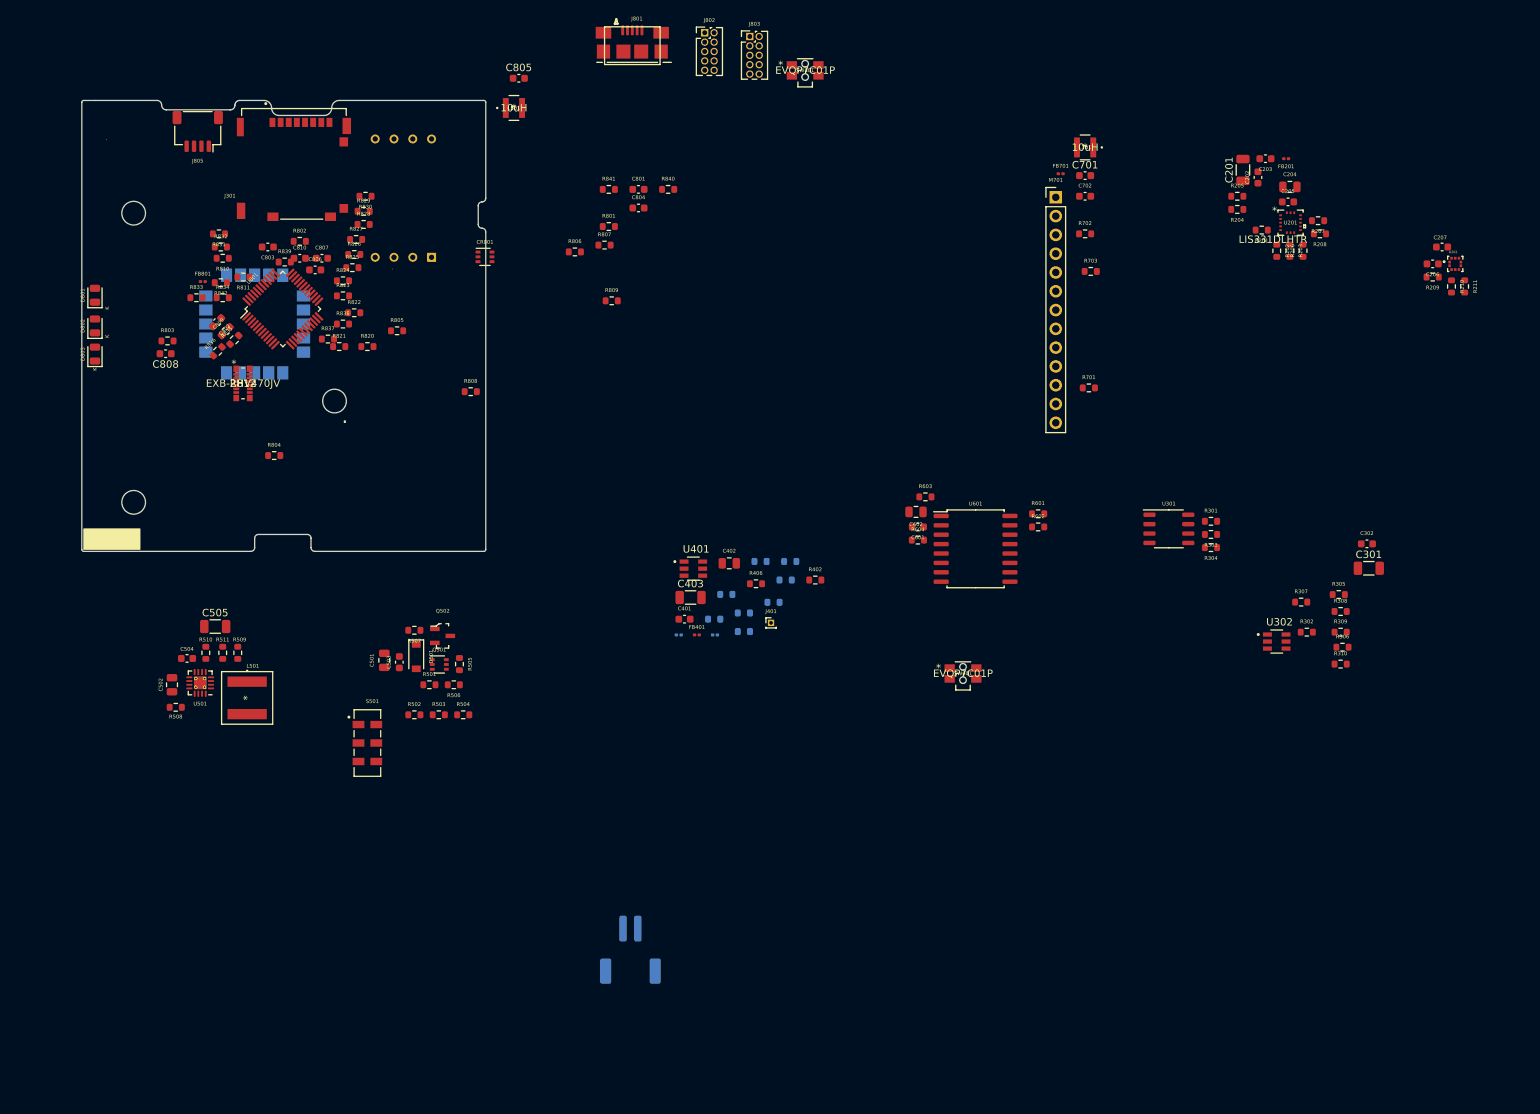
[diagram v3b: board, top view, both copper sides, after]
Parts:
- removed R813, R814, R815, R816, R817, R818, R819: 47, Resistor_SMD:R_0603_1608Metric
- FB402, FB403, J501, R401, R403, R404, R405, R407, R408, R409, R410: moved to B.Cu
- R812: value 47 -> EXB-2HV470JV; footprint Resistor_SMD:R_0603_1608Metric -> SapphineMinimal:EXB-2HV470JV
- moved L501 175.4 mm to (99.3, 146.8), turned to -90 degrees
- moved R502 167.1 mm to (121.9, 149.1)
- moved M701 165.9 mm to (208.6, 79.1)
- moved R503 157.7 mm to (125.2, 149.1)
- moved Q502 154.6 mm to (125.7, 138.4)
- moved R504 153.7 mm to (128.5, 149.1)
- moved C203 123.6 mm to (237.0, 73.9), turned to 180 degrees
- moved C205 116.0 mm to (240.0, 79.8)
- moved R205 114.4 mm to (233.2, 79.0)
- moved R201 109.1 mm to (236.5, 83.6), turned to 180 degrees
- moved U201 107.8 mm to (240.4, 82.6)
- moved R204 107.1 mm to (233.2, 80.8), turned to 180 degrees
- moved R206 106.3 mm to (242.1, 86.4), turned to 90 degrees
- moved C202 105.2 mm to (236.0, 76.5), turned to 90 degrees
- moved C201 105.2 mm to (233.9, 75.4), turned to 90 degrees
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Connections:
- R407 pad 2: /SapphireMini_GNSS/GNSS_RESET -> /Sapphire_Proc/PA21
- R812 pad 1: Net-(R812-Pad1) -> /Sapphire_Proc/32KHz
- R812 pad 2: /Sapphire_Proc/32KHz -> /Sapphire_Proc/RED_LED
- R820 pad 2: /Sapphire_Proc/AUX2 -> /Sapphire_Proc/PA13
- R825 pad 2: /Sapphire_Proc/AUX3 -> /Sapphire_Proc/PA20
- R826 pad 2: /SapphireMini_GNSS/GNSS_RESET -> /Sapphire_Proc/PA21
- U801 pad 1: Net-(R812-Pad1) -> /Sapphire_Proc/PA00
- U801 pad 10: Net-(R815-Pad1) -> /Sapphire_Proc/PA05
- U801 pad 11: Net-(R816-Pad1) -> /Sapphire_Proc/PA06
- U801 pad 12: Net-(R817-Pad1) -> /Sapphire_Proc/PA07
- U801 pad 14: Net-(R818-Pad1) -> /Sapphire_Proc/PA09
- U801 pad 21: Net-(R819-Pad1) -> unconnected-(U801-Pad21)
- U801 pad 3: Net-(R813-Pad1) -> /Sapphire_Proc/PA02
- U801 pad 9: Net-(R814-Pad1) -> /Sapphire_Proc/PA04
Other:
- board size 170.9 x 133.9 mm -> 54.6 x 61 mm
